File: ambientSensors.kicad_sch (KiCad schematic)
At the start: 10 parts, among them Q3 PMH950UPEH, U1 LTR-329ALS-01, U2 SHT40-AD1F-R2, U3 ZMOD4410AI1R

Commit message: 2nd rev schematic done
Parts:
- removed Q3: PMH950UPEH, SproutSenseFootprints:QPMOS1G2S3d_SOT8001_NEX, symbol SproutSense:PMH950UPEH
- removed TP4, TP5, TP6, TP7: TestPoint, symbol Connector:TestPoint
- added C12: 1uF, Capacitor_SMD:C_0402_1005Metric, symbol Device:C_Small
- added Q6: SIUD412ED-T1-GE3, SMT_412ED-T1-GE3_VIS, symbol SproutSense:SIUD412ED-T1-GE3
- added R14, R19, R20: 4.7k, Resistor_SMD:R_0402_1005Metric, symbol Device:R_Small_US
- added TP10, TP11, TP12, TP9: TestPoint, symbol Connector:TestPoint
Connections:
- net Sns_3p3 is gone; now on net +3V3: C1.1, C2.1, U1.1 (VDD), U2.3 (VDD), U3.10 (VDDH), U3.12 (VDDIO), U3.5 (VDD)
- net +3V3: now also C12.1, R19.2, R20.2
- net GAS_INT: now also TP11.1
- net GND: now also Q6.2 (S), R14.1; no longer C1.2, C2.2, U1.2 (GND), U2.4 (VSS), U3.6 (VSS), U3.7 (VSS), U3.9 (VSS)
- net I2C_SCL: now also R20.1, TP10.1
- net I2C_SDA: now also R19.1, TP9.1
- net ~{nGAS_RES}: now also TP12.1
- new net AMB_SNS_ENA: Q6.1 (G), R14.2
- new net GND2: C1.2, C12.2, C2.2, Q6.3 (D), U1.2 (GND), U2.4 (VSS), U3.6 (VSS), U3.7 (VSS), U3.9 (VSS)

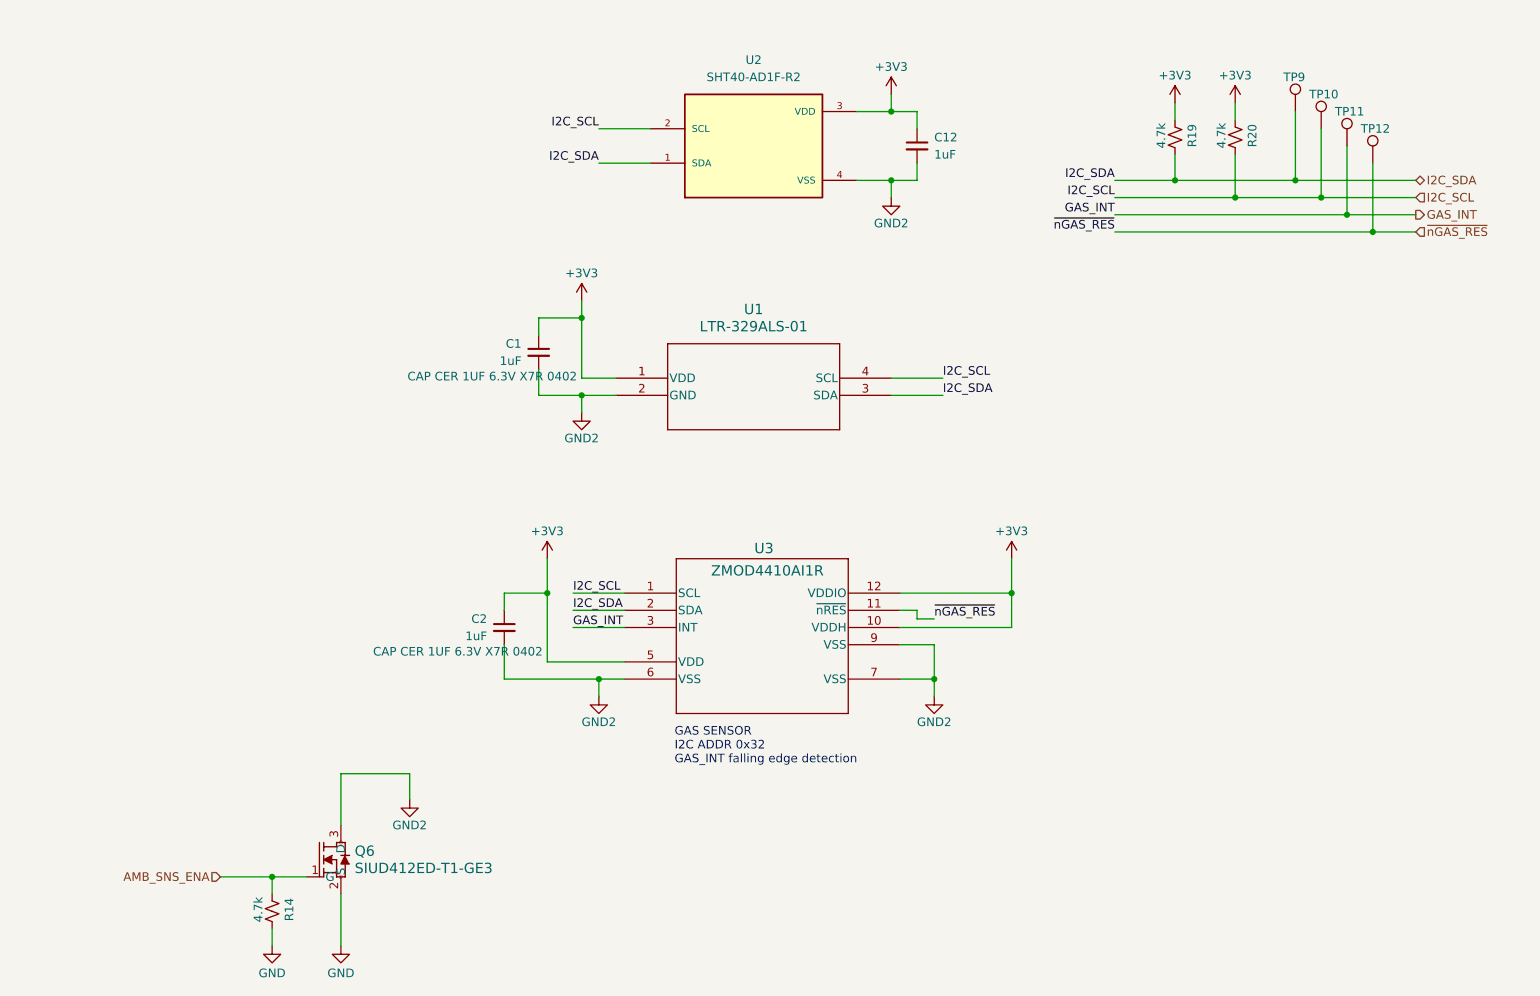
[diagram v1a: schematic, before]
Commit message: mostly routed
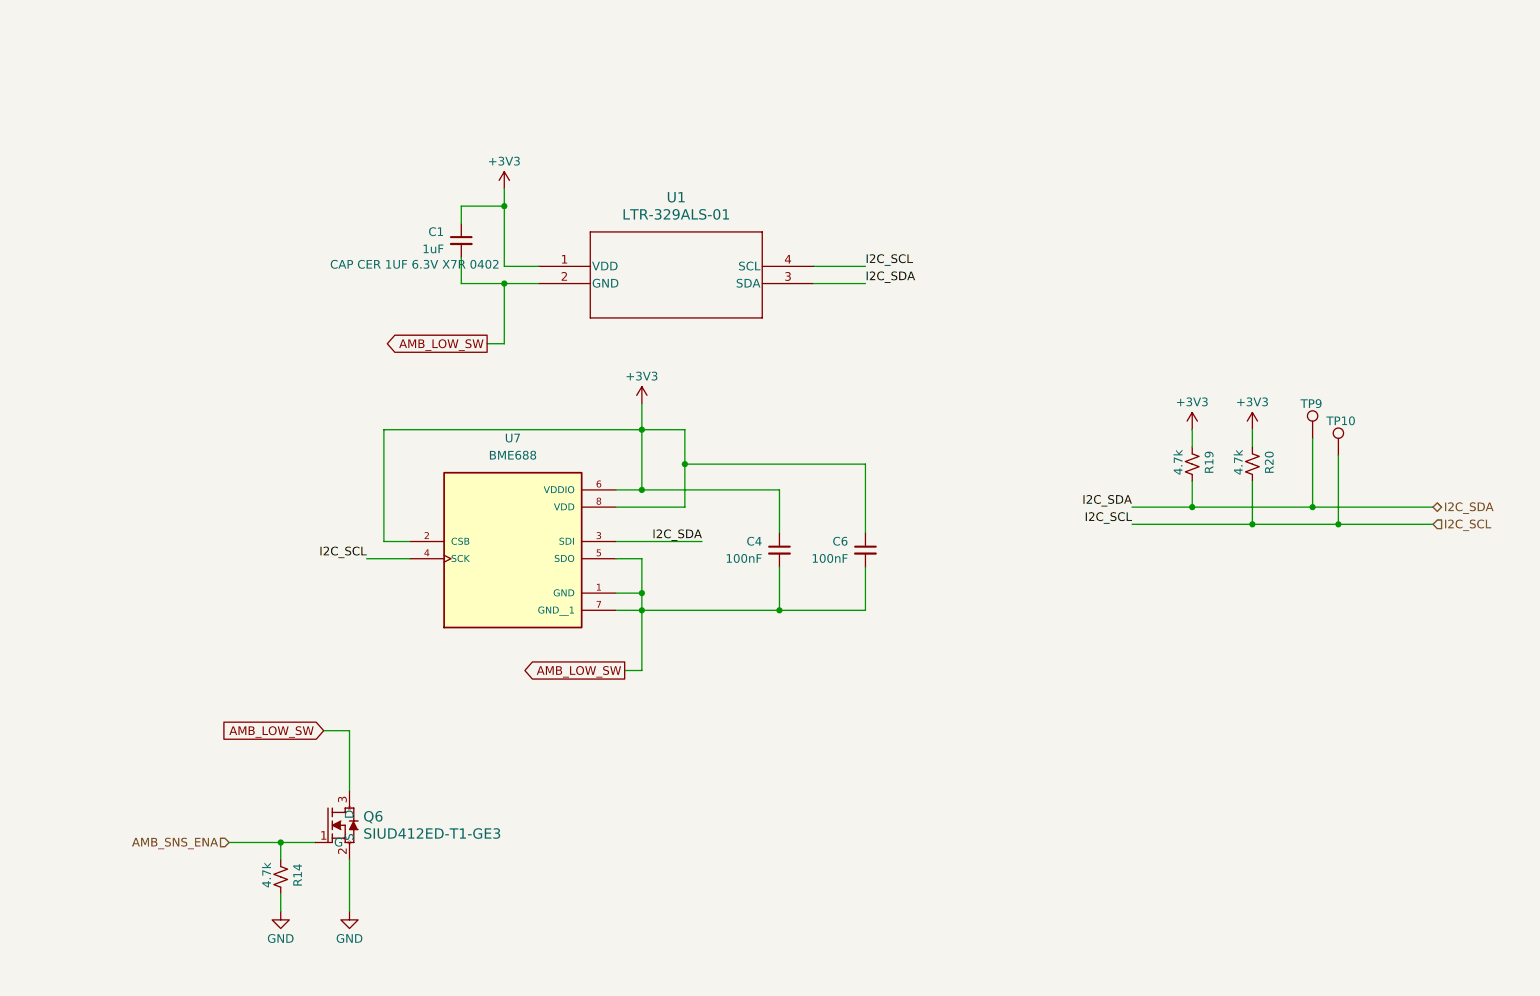
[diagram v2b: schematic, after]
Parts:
- removed C12, C2: 1uF, Capacitor_SMD:C_0402_1005Metric, symbol Device:C_Small
- removed TP11, TP12: TestPoint, symbol Connector:TestPoint
- removed U2: SHT40-AD1F-R2, SproutSenseFootprints:SHT4X, symbol SproutSense:SHT40-AD1F-R2
- removed U3: ZMOD4410AI1R, SproutSenseFootprints:QFN_410AI1R_REN, symbol SproutSense:ZMOD4410AI1R
- added C4, C6: 100nF, Capacitor_SMD:C_0402_1005Metric, symbol Device:C_Small
- added U7: BME688, SproutSenseFootprints:IC_BME688, symbol SproutSense:BME688
- Q6: Distributor Prt # (none) -> SIUD412ED-T1-GE3CT-ND; Manuf Prt # (none) -> SIUD412ED-T1-GE3
- TP10, TP9: footprint (none) -> TestPoint:TestPoint_Pad_D1.0mm
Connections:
- net +3V3: now also C4.1, C6.1, U7.2 (CSB), U7.6 (VDDIO), U7.8 (VDD)
- net I2C_SCL: now also U7.4 (SCK)
- net I2C_SDA: now also U7.3 (SDI)
- net GND2 renamed AMB_LOW_SW
- net AMB_LOW_SW: now also C4.2, C6.2, U7.1 (GND), U7.5 (SDO), U7.7 (GND__1)
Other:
- note removed: "GAS SENSOR I2C ADDR 0x32 GAS_INT falling edge detection"
- moved on the sheet: C1, Q6, R14, R19, R20, TP10, TP9, U1

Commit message: Removed via in pads
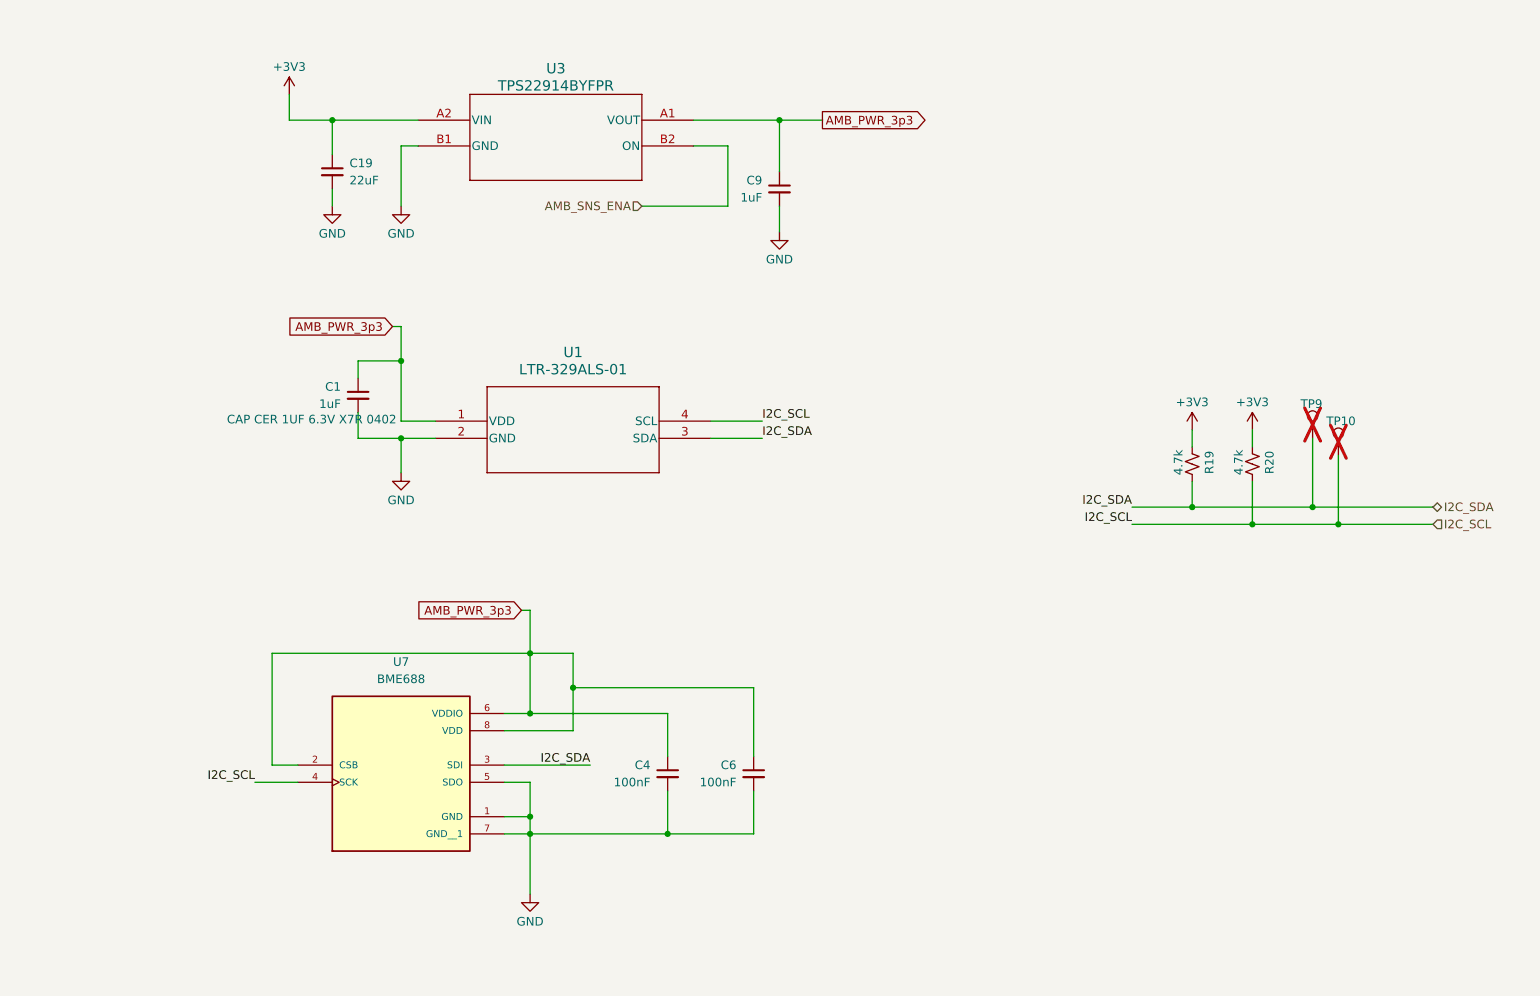
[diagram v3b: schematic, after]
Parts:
- removed Q6: SIUD412ED-T1-GE3, SMT_412ED-T1-GE3_VIS, symbol SproutSense:SIUD412ED-T1-GE3
- removed R14: 4.7k, Resistor_SMD:R_0402_1005Metric, symbol Device:R_Small_US
- added C19: 22uF, Capacitor_SMD:C_0402_1005Metric, symbol Device:C_Small
- added C9: 1uF, Capacitor_SMD:C_0402_1005Metric, symbol Device:C_Small
- added U3: TPS22914BYFPR, SproutSenseFootprints:YFP4_TEX, symbol SproutSense:TPS22914BYFPR
- TP10, TP9: now not fitted; now left out of the parts list
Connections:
- net AMB_LOW_SW is gone; now on net GND: C1.2, C4.2, C6.2, U1.2 (GND), U7.1 (GND), U7.5 (SDO), U7.7 (GND__1)
- net +3V3: now also C19.1, U3.A2 (VIN); no longer C1.1, C4.1, C6.1, U1.1 (VDD), U7.2 (CSB), U7.6 (VDDIO), U7.8 (VDD)
- net AMB_SNS_ENA: now also U3.B2 (ON)
- net GND: now also C19.2, C9.2, U3.B1 (GND)
- new net AMB_PWR_3p3: C1.1, C4.1, C6.1, C9.1, U1.1 (VDD), U3.A1 (VOUT), U7.2 (CSB), U7.6 (VDDIO), U7.8 (VDD)
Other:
- moved on the sheet: C1, C4, C6, U1, U7
